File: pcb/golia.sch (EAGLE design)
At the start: 23 parts, among them IC1 xm64a4u, IC2 LM340MP, X2 EXT

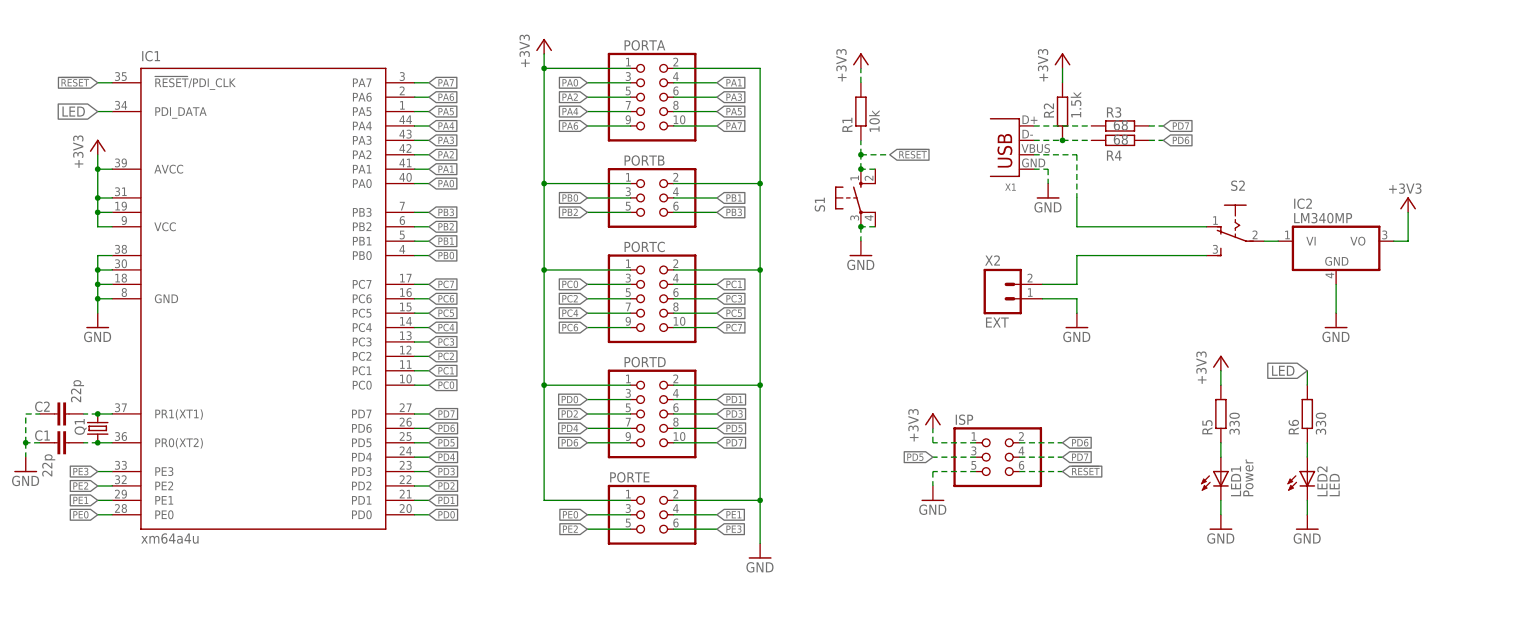
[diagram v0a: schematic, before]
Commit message: Changed component packages
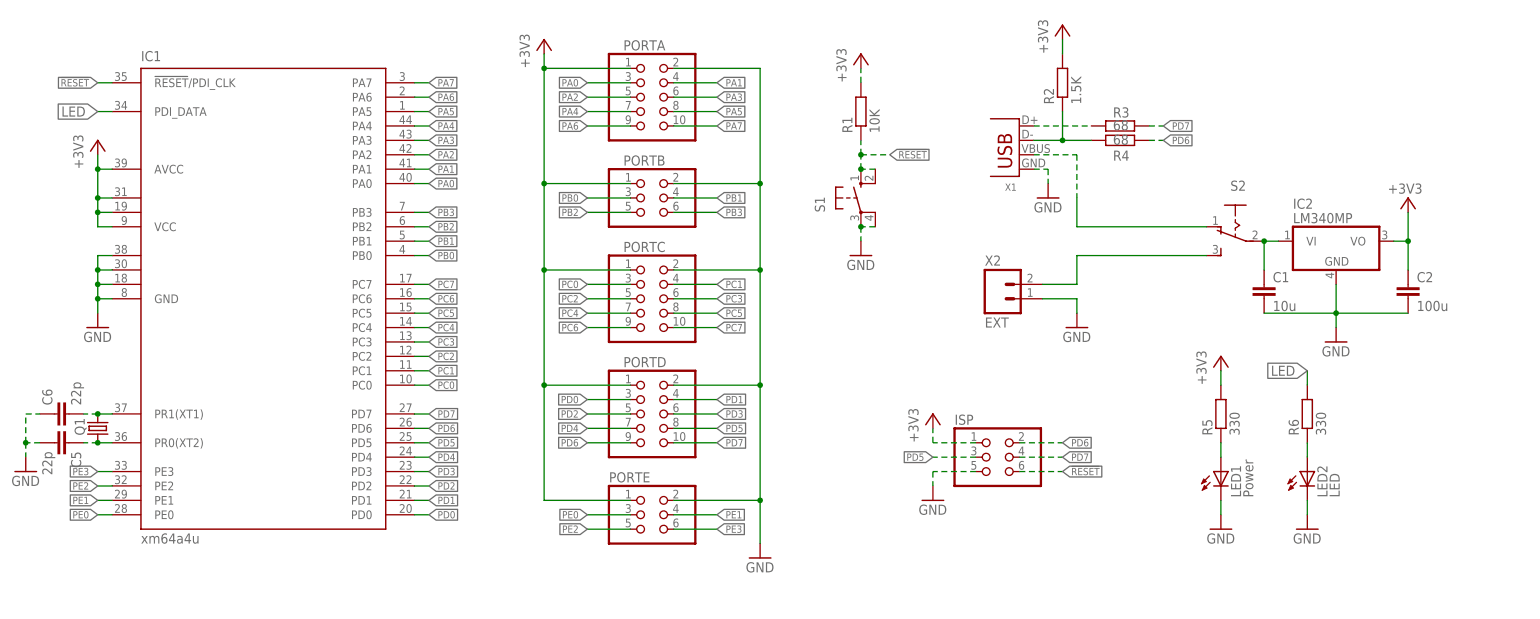
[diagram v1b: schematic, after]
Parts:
- added C5, C6: 22p, Passives:C0603
- C1: value 22p -> 10u; device resistor:C-EU025-024X044 -> Passives:C0603
- C2: value 22p -> 100u; device resistor:C-EU025-024X044 -> rcl:C-EUC1206
- R1: value 10k -> 10K; device resistor:R-EU_M0805 -> rcl:R-EU_R0603
- R2: value 1.5k -> 1.5K; device resistor:R-EU_M0805 -> rcl:R-EU_R0603
- R3, R4: device resistor:R-EU_M0805 -> rcl:R-EU_R0603
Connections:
- net +3V3: now also C2.1
- net GND: now also C1.2, C2.2, C5.2, C6.1; no longer C1.1, C2.1
- net N$23: now also C5.1; no longer C1.2
- net N$24: now also C6.2; no longer C2.2
- net N$5: now also C1.1
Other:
- moved on the sheet: C1, C2, R2

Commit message: Changed layout of board, USB now central
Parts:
- R5, R6: device resistor:R-EU_M0805 -> rcl:R-EU_R0603
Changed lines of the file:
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@@
 <part name="GND1" library="supply1" deviceset="GND" device=""/>
 <part name="GND9" library="supply1" deviceset="GND" device=""/>
-<part name="R5" library="resistor" deviceset="R-EU_" device="M0805" value="330"/>
-<part name="R6" library="resistor" deviceset="R-EU_" device="M0805" value="330"/>
+<part name="R5" library="rcl" deviceset="R-EU_" device="R0603" value="330"/>
+<part name="R6" library="rcl" deviceset="R-EU_" device="R0603" value="330"/>
 <part name="LED1" library="led" deviceset="LED" device="CHIP-LED0805" value="Power"/>
 <part name="LED2" library="led" deviceset="LED" device="CHIP-LED0805" value="LED"/>

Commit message: Added Silkscreen for ports
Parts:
- LED1: value Power -> PWR
- renumbered PORTA to A, PORTB to B, PORTC to C, PORTD to D, PORTE to E

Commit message: * Swapped out the power switch, regulator, and USB connector with those available free from the uni * Fattened up some of the power supply traces.
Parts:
- removed IC2: LM340MP, linear:LM340MP-05
- removed S2: (no value), switch:255SB
- removed X1: (no value), con-usb-3:USB-MB-S
- added S3: SPDTEG-1218, Switches:SPDTEG-1218
- added U$1: USB-MINIB-PTH, Connectors:USB-MINIB-PTH
- added U1: MCP1825S-3302E/DB, mcp1825:MCP1825S-3302E/DB
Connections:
- net +3V3: now also U1.VOUT; no longer IC2.VO
- net GND: now also U$1.GND, U$1.SHD1, U$1.SHD2, U1.GND, U1.GND_TAB; no longer IC2.GND, X1.GND
- net N$1: now also S3.1; no longer S2.S
- net N$2: now also S3.2, U$1.VBUS; no longer S2.O, X1.VBUS
- net N$3: now also U$1.D-; no longer X1.D-
- net N$4: now also U$1.D+; no longer X1.D+
- net N$5: now also S3.C, U1.VIN; no longer IC2.VI, S2.P
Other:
- moved on the sheet: C1, C2, ISP, LED1, LED2, R5, R6

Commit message: Added names to silk screen increased board size to fit port silks
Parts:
- S: value SPDTEG-1218 -> 3
- renumbered S3 to S
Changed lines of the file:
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@@
 <?xml version="1.0" encoding="utf-8"?>
 <!DOCTYPE eagle SYSTEM "eagle.dtd">
-<eagle version="7.7.0">
+<eagle version="8.1.0">
 <drawing>
 <settings>
@@
 <part name="R3" library="rcl" deviceset="R-EU_" device="R0603" value="68"/>
 <part name="R4" library="rcl" deviceset="R-EU_" device="R0603" value="68"/>
-<part name="S3" library="Switches" deviceset="SPDT" device="EG-1218"/>
+<part name="S" library="Switches" deviceset="SPDT" device="EG-1218" value="3"/>
 <part name="U$1" library="Connectors" deviceset="USB-MINI" device="B-PTH"/>
 <part name="GND10" library="supply1" deviceset="GND" device=""/>
@@
 <attribute name="VALUE" x="171.45" y="67.818" size="1.778" layer="96"/>
 </instance>
-<instance part="S3" gate="G$1" x="193.04" y="50.8" rot="R180"/>
+<instance part="S" gate="G$1" x="193.04" y="50.8" rot="R180"/>
 <instance part="U$1" gate="G$1" x="152.4" y="66.04" rot="MR0"/>
 <instance part="GND10" gate="1" x="147.32" y="53.34"/>
@@
 <wire x1="165.1" y1="58.42" x2="165.1" y2="53.34" width="0.1524" layer="91"/>
 <wire x1="165.1" y1="53.34" x2="187.96" y2="53.34" width="0.1524" layer="91"/>
-<pinref part="S3" gate="G$1" pin="2"/>
+<pinref part="S" gate="G$1" pin="2"/>
 <pinref part="U$1" gate="G$1" pin="VBUS"/>
 </segment>
@@
 <pinref part="X2" gate="G$1" pin="2"/>
 <wire x1="159.004" y1="43.18" x2="165.1" y2="43.18" width="0.1524" layer="91"/>
-<pinref part="S3" gate="G$1" pin="1"/>
+<pinref part="S" gate="G$1" pin="1"/>
 </segment>
 </net>
@@
 <wire x1="198.12" y1="40.64" x2="198.12" y2="50.8" width="0.1524" layer="91"/>
 <pinref part="C1" gate="G$1" pin="1"/>
-<pinref part="S3" gate="G$1" pin="C"/>
+<pinref part="S" gate="G$1" pin="C"/>
 <junction x="198.12" y="50.8"/>
 <pinref part="U1" gate="A" pin="VIN"/>

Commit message: Changes to LEDs
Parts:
- removed C5, C6: 22p, Passives:C0603
- removed Q1: (no value), adafruit:CRYSTALCTS406
- added LED3: LED1, led:LEDCHIP-LED0805
- added R7: 330, rcl:R-EU_R0603
- LED2: value LED -> LED2
- renumbered U$1 to USB
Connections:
- removed net LED: IC1.PDI_DATA, R6.2
- removed net N$23: C5.1, IC1.PR0(XT2), Q1.1
- removed net N$24: C6.2, IC1.PR1(XT1), Q1.2
- new net LED1: IC1.PR1(XT1), R6.2
- new net LED2: IC1.PR0(XT2), R7.2
- new net N$10: LED3.A, R7.1
- net GND: now also LED3.C; no longer C5.2, C6.1
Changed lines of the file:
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@@
 <part name="+3V4" library="supply1" deviceset="+3V3" device=""/>
 <part name="GND4" library="supply1" deviceset="GND" device=""/>
-<part name="GND5" library="supply1" deviceset="GND" device=""/>
-<part name="Q1" library="adafruit" deviceset="CRYSTAL" device="CTS406"/>
 <part name="GND6" library="supply1" deviceset="GND" device=""/>
 <part name="+3V5" library="supply1" deviceset="+3V3" device=""/>
@@
 <part name="R6" library="rcl" deviceset="R-EU_" device="R0603" value="330"/>
 <part name="LED1" library="led" deviceset="LED" device="CHIP-LED0805" value="PWR"/>
-<part name="LED2" library="led" deviceset="LED" device="CHIP-LED0805" value="LED"/>
-<part name="C5" library="Passives" deviceset="C" device="0603" value="22p"/>
-<part name="C6" library="Passives" deviceset="C" device="0603" value="22p"/>
+<part name="LED2" library="led" deviceset="LED" device="CHIP-LED0805" value="LED2"/>
 <part name="C1" library="Passives" deviceset="C" device="0603" value="10u"/>
 <part name="C2" library="rcl" deviceset="C-EU" device="C1206" value="100u"/>
@@
 <part name="R4" library="rcl" deviceset="R-EU_" device="R0603" value="68"/>
 <part name="S" library="Switches" deviceset="SPDT" device="EG-1218" value="3"/>
-<part name="U$1" library="Connectors" deviceset="USB-MINI" device="B-PTH"/>
+<part name="USB" library="Connectors" deviceset="USB-MINI" device="B-PTH"/>
 <part name="GND10" library="supply1" deviceset="GND" device=""/>
 <part name="GND11" library="supply1" deviceset="GND" device=""/>
 <part name="U1" library="mcp1825" deviceset="MCP1825S-3302E/DB" device=""/>
+<part name="R7" library="rcl" deviceset="R-EU_" device="R0603" value="330"/>
+<part name="LED3" library="led" deviceset="LED" device="CHIP-LED0805" value="LED1"/>
+<part name="GND5" library="supply1" deviceset="GND" device=""/>
 </parts>
 <sheets>
@@
 <instance part="+3V4" gate="G$1" x="139.7" y="10.16"/>
 <instance part="GND4" gate="1" x="139.7" y="-5.08"/>
-<instance part="GND5" gate="1" x="-20.32" y="10.16"/>
-<instance part="Q1" gate="G$1" x="-7.62" y="17.78" smashed="yes" rot="R90">
-<attribute name="NAME" x="-9.906" y="16.51" size="1.778" layer="95" rot="R90"/>
-<attribute name="VALUE" x="-5.08" y="20.32" size="1.778" layer="96" rot="R90"/>
-</instance>
 <instance part="GND6" gate="1" x="160.02" y="58.42"/>
 <instance part="+3V5" gate="G$1" x="162.56" y="88.9"/>
@@
 <instance part="LED1" gate="G$1" x="190.5" y="0"/>
 <instance part="LED2" gate="G$1" x="205.74" y="0"/>
-<instance part="C5" gate="G$1" x="-12.7" y="15.24" rot="R270"/>
-<instance part="C6" gate="G$1" x="-15.24" y="20.32" rot="R90"/>
 <instance part="C1" gate="G$1" x="198.12" y="38.1"/>
 <instance part="C2" gate="G$1" x="236.22" y="38.1"/>
@@
 </instance>
 <instance part="S" gate="G$1" x="193.04" y="50.8" rot="R180"/>
-<instance part="U$1" gate="G$1" x="152.4" y="66.04" rot="MR0"/>
+<instance part="USB" gate="G$1" x="152.4" y="66.04" smashed="yes" rot="MR0">
+<attribute name="NAME" x="144.78" y="73.66" size="1.778" layer="95" rot="MR0"/>
+</instance>
 <instance part="GND10" gate="1" x="147.32" y="53.34"/>
 <instance part="GND11" gate="1" x="152.4" y="76.2"/>
 <instance part="U1" gate="A" x="220.98" y="53.34"/>
+<instance part="R7" gate="G$1" x="220.98" y="10.16" rot="R90"/>
+<instance part="LED3" gate="G$1" x="220.98" y="0"/>
+<instance part="GND5" gate="1" x="220.98" y="-10.16"/>
 </instances>
 <busses>
@@
 </segment>
 <segment>
-<wire x1="-17.78" y1="15.24" x2="-20.32" y2="15.24" width="0.1524" layer="91" style="longdash"/>
-<wire x1="-20.32" y1="15.24" x2="-20.32" y2="20.32" width="0.1524" layer="91" style="longdash"/>
-<wire x1="-20.32" y1="20.32" x2="-17.78" y2="20.32" width="0.1524" layer="91" style="longdash"/>
-<wire x1="-20.32" y1="15.24" x2="-20.32" y2="12.7" width="0.1524" layer="91" style="longdash"/>
-<junction x="-20.32" y="15.24"/>
-<pinref part="GND5" gate="1" pin="GND"/>
-<pinref part="C6" gate="G$1" pin="1"/>
-<pinref part="C5" gate="G$1" pin="2"/>
-</segment>
-<segment>
 <wire x1="157.48" y1="63.5" x2="160.02" y2="63.5" width="0.1524" layer="91" style="longdash"/>
 <wire x1="160.02" y1="63.5" x2="160.02" y2="60.96" width="0.1524" layer="91" style="longdash"/>
 <pinref part="GND6" gate="1" pin="GND"/>
-<pinref part="U$1" gate="G$1" pin="GND"/>
+<pinref part="USB" gate="G$1" pin="GND"/>
 </segment>
 <segment>
@@
 <pinref part="GND11" gate="1" pin="GND"/>
 <wire x1="152.4" y1="81.28" x2="152.4" y2="78.74" width="0.1524" layer="91"/>
-<pinref part="U$1" gate="G$1" pin="SHD1"/>
-</segment>
-<segment>
-<pinref part="U$1" gate="G$1" pin="SHD2"/>
+<pinref part="USB" gate="G$1" pin="SHD1"/>
+</segment>
+<segment>
+<pinref part="USB" gate="G$1" pin="SHD2"/>
 <pinref part="GND10" gate="1" pin="GND"/>
 <wire x1="147.32" y1="57.15" x2="147.32" y2="55.88" width="0.1524" layer="91"/>
+</segment>
+<segment>
+<pinref part="GND5" gate="1" pin="GND"/>
+<pinref part="LED3" gate="G$1" pin="C"/>
+<wire x1="220.98" y1="-7.62" x2="220.98" y2="-5.08" width="0.1524" layer="91"/>
 </segment>
 </net>
@@
 <wire x1="101.6" y1="2.54" x2="93.98" y2="2.54" width="0.1524" layer="91"/>
 <label x="101.6" y="2.54" size="1.27" layer="95" xref="yes"/>
-</segment>
-</net>
-<net name="N$23" class="0">
-<segment>
-<pinref part="IC1" gate="G$1" pin="PR0(XT2)"/>
-<wire x1="-5.08" y1="15.24" x2="-7.62" y2="15.24" width="0.1524" layer="91"/>
-<wire x1="-7.62" y1="15.24" x2="-10.16" y2="15.24" width="0.1524" layer="91" style="longdash"/>
-<pinref part="Q1" gate="G$1" pin="1"/>
-<junction x="-7.62" y="15.24"/>
-<pinref part="C5" gate="G$1" pin="1"/>
-</segment>
-</net>
-<net name="N$24" class="0">
-<segment>
-<pinref part="IC1" gate="G$1" pin="PR1(XT1)"/>
-<wire x1="-5.08" y1="20.32" x2="-7.62" y2="20.32" width="0.1524" layer="91"/>
-<wire x1="-7.62" y1="20.32" x2="-10.16" y2="20.32" width="0.1524" layer="91" style="longdash"/>
-<pinref part="Q1" gate="G$1" pin="2"/>
-<junction x="-7.62" y="20.32"/>
-<pinref part="C6" gate="G$1" pin="2"/>
 </segment>
 </net>
@@
 <wire x1="165.1" y1="53.34" x2="187.96" y2="53.34" width="0.1524" layer="91"/>
 <pinref part="S" gate="G$1" pin="2"/>
-<pinref part="U$1" gate="G$1" pin="VBUS"/>
+<pinref part="USB" gate="G$1" pin="VBUS"/>
 </segment>
 </net>
@@
 <wire x1="157.48" y1="71.12" x2="167.64" y2="71.12" width="0.1524" layer="91" style="longdash"/>
 <pinref part="R3" gate="G$1" pin="1"/>
-<pinref part="U$1" gate="G$1" pin="D+"/>
+<pinref part="USB" gate="G$1" pin="D+"/>
 </segment>
 </net>
@@
 </segment>
 </net>
-<net name="LED" class="0">
-<segment>
-<pinref part="IC1" gate="G$1" pin="PDI_DATA"/>
-<wire x1="-5.08" y1="73.66" x2="-7.62" y2="73.66" width="0.1524" layer="91"/>
-<label x="-7.62" y="73.66" size="1.778" layer="95" rot="MR0" xref="yes"/>
-</segment>
-<segment>
-<pinref part="R6" gate="G$1" pin="2"/>
-<wire x1="205.74" y1="15.24" x2="205.74" y2="17.78" width="0.1524" layer="91"/>
-<label x="205.74" y="17.78" size="1.778" layer="95" rot="R180" xref="yes"/>
-</segment>
-</net>
 <net name="N$3" class="0">
 <segment>
@@
 <pinref part="R2" gate="G$1" pin="1"/>
 <pinref part="R4" gate="G$1" pin="1"/>
-<pinref part="U$1" gate="G$1" pin="D-"/>
-</segment>
-</net>
+<pinref part="USB" gate="G$1" pin="D-"/>
+</segment>
+</net>
+<net name="LED1" class="0">
+<segment>
+<pinref part="IC1" gate="G$1" pin="PR1(XT1)"/>
+<wire x1="-5.08" y1="20.32" x2="-7.62" y2="20.32" width="0.1524" layer="91"/>
+<label x="-7.62" y="20.32" size="1.778" layer="95" rot="R180" xref="yes"/>
+</segment>
+<segment>
+<pinref part="R6" gate="G$1" pin="2"/>
+<wire x1="205.74" y1="15.24" x2="205.74" y2="17.78" width="0.1524" layer="91"/>
+<label x="205.74" y="17.78" size="1.778" layer="95" rot="R180" xref="yes"/>
+<wire x1="205.74" y1="15.24" x2="205.74" y2="17.78" width="0.1524" layer="91"/>
+</segment>
+</net>
+<net name="LED2" class="0">
+<segment>
+<pinref part="IC1" gate="G$1" pin="PR0(XT2)"/>
+<wire x1="-5.08" y1="15.24" x2="-7.62" y2="15.24" width="0.1524" layer="91"/>
+<label x="-7.62" y="15.24" size="1.778" layer="95" rot="R180" xref="yes"/>
+</segment>
+<segment>
+<pinref part="R7" gate="G$1" pin="2"/>
+<wire x1="220.98" y1="15.24" x2="220.98" y2="17.78" width="0.1524" layer="91"/>
+<label x="220.98" y="17.78" size="1.778" layer="95" rot="R180" xref="yes"/>
+</segment>
+</net>
+<net name="N$10" class="0">
+<segment>
+<pinref part="R7" gate="G$1" pin="1"/>
+<pinref part="LED3" gate="G$1" pin="A"/>
+<wire x1="220.98" y1="5.08" x2="220.98" y2="2.54" width="0.1524" layer="91"/>
+</segment>
+</net>

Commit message: Reduced width and removed !RST pullup
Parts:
- removed R1: 10K, rcl:R-EU_R0603
- S3: value 3 -> S3
- renumbered S to S3
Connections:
- net !RESET: no longer R1.1
- net +3V3: no longer R1.2
- net LED1: now also IC1.PR0(XT2), R7.2; no longer IC1.PR1(XT1), R6.2
- net LED2: now also IC1.PR1(XT1), R6.2; no longer IC1.PR0(XT2), R7.2
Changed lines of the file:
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@@
 <part name="A" library="pinhead" deviceset="PINHD-2X5" device=""/>
 <part name="S1" library="switch-omron" deviceset="10-XX" device=""/>
-<part name="+3V3" library="supply1" deviceset="+3V3" device=""/>
 <part name="GND3" library="supply1" deviceset="GND" device=""/>
 <part name="ISP" library="pinhead" deviceset="PINHD-2X3" device=""/>
@@
 <part name="C1" library="Passives" deviceset="C" device="0603" value="10u"/>
 <part name="C2" library="rcl" deviceset="C-EU" device="C1206" value="100u"/>
-<part name="R1" library="rcl" deviceset="R-EU_" device="R0603" value="10K"/>
 <part name="R2" library="rcl" deviceset="R-EU_" device="R0603" value="1.5K"/>
 <part name="R3" library="rcl" deviceset="R-EU_" device="R0603" value="68"/>
 <part name="R4" library="rcl" deviceset="R-EU_" device="R0603" value="68"/>
-<part name="S" library="Switches" deviceset="SPDT" device="EG-1218" value="3"/>
+<part name="S3" library="Switches" deviceset="SPDT" device="EG-1218" value="S3"/>
 <part name="USB" library="Connectors" deviceset="USB-MINI" device="B-PTH"/>
 <part name="GND10" library="supply1" deviceset="GND" device=""/>
@@
 </instance>
 <instance part="E" gate="A" x="88.9" y="2.54" smashed="yes">
-<attribute name="NAME" x="82.55" y="8.255" size="1.778" layer="95"/>
+<attribute name="NAME" x="85.09" y="8.255" size="1.778" layer="95"/>
 <attribute name="VALUE" x="82.55" y="-5.08" size="1.778" layer="96"/>
 </instance>
@@
 </instance>
 <instance part="S1" gate="1" x="127" y="58.42"/>
-<instance part="+3V3" gate="G$1" x="127" y="83.82"/>
 <instance part="GND3" gate="1" x="127" y="48.26"/>
 <instance part="ISP" gate="A" x="149.86" y="2.54"/>
@@
 <instance part="C1" gate="G$1" x="198.12" y="38.1"/>
 <instance part="C2" gate="G$1" x="236.22" y="38.1"/>
-<instance part="R1" gate="G$1" x="127" y="73.66" rot="R90"/>
 <instance part="R2" gate="G$1" x="162.56" y="78.74" rot="R90"/>
 <instance part="R3" gate="G$1" x="172.72" y="71.12" smashed="yes">
@@
 <attribute name="VALUE" x="171.45" y="67.818" size="1.778" layer="96"/>
 </instance>
-<instance part="S" gate="G$1" x="193.04" y="50.8" rot="R180"/>
+<instance part="S3" gate="G$1" x="193.04" y="50.8" rot="R180"/>
 <instance part="USB" gate="G$1" x="152.4" y="66.04" smashed="yes" rot="MR0">
 <attribute name="NAME" x="144.78" y="73.66" size="1.778" layer="95" rot="MR0"/>
@@
 </segment>
 <segment>
-<wire x1="127" y1="78.74" x2="127" y2="81.28" width="0.1524" layer="91" style="longdash"/>
-<pinref part="+3V3" gate="G$1" pin="+3V3"/>
-<pinref part="R1" gate="G$1" pin="2"/>
-</segment>
-<segment>
 <pinref part="ISP" gate="A" pin="1"/>
 <wire x1="147.32" y1="5.08" x2="139.7" y2="5.08" width="0.1524" layer="91" style="longdash"/>
@@
 <wire x1="129.54" y1="63.5" x2="127" y2="63.5" width="0.1524" layer="91" style="longdash"/>
 <junction x="127" y="63.5"/>
-<wire x1="127" y1="63.5" x2="127" y2="66.04" width="0.1524" layer="91" style="longdash"/>
-<wire x1="127" y1="66.04" x2="127" y2="68.58" width="0.1524" layer="91" style="longdash"/>
-<wire x1="127" y1="66.04" x2="132.08" y2="66.04" width="0.1524" layer="91" style="longdash"/>
-<junction x="127" y="66.04"/>
-<label x="132.08" y="66.04" size="1.27" layer="95" xref="yes"/>
-<pinref part="R1" gate="G$1" pin="1"/>
+<wire x1="127" y1="63.5" x2="127" y2="71.12" width="0.1524" layer="91" style="longdash"/>
+<label x="127" y="71.12" size="1.27" layer="95" rot="R180" xref="yes"/>
 </segment>
 </net>
@@
 <wire x1="165.1" y1="58.42" x2="165.1" y2="53.34" width="0.1524" layer="91"/>
 <wire x1="165.1" y1="53.34" x2="187.96" y2="53.34" width="0.1524" layer="91"/>
-<pinref part="S" gate="G$1" pin="2"/>
+<pinref part="S3" gate="G$1" pin="2"/>
 <pinref part="USB" gate="G$1" pin="VBUS"/>
 </segment>
@@
 <pinref part="X2" gate="G$1" pin="2"/>
 <wire x1="159.004" y1="43.18" x2="165.1" y2="43.18" width="0.1524" layer="91"/>
-<pinref part="S" gate="G$1" pin="1"/>
+<pinref part="S3" gate="G$1" pin="1"/>
 </segment>
 </net>
@@
 <wire x1="198.12" y1="40.64" x2="198.12" y2="50.8" width="0.1524" layer="91"/>
 <pinref part="C1" gate="G$1" pin="1"/>
-<pinref part="S" gate="G$1" pin="C"/>
+<pinref part="S3" gate="G$1" pin="C"/>
 <junction x="198.12" y="50.8"/>
 <pinref part="U1" gate="A" pin="VIN"/>
@@
 </segment>
 </net>
-<net name="LED1" class="0">
+<net name="LED2" class="0">
 <segment>
 <pinref part="IC1" gate="G$1" pin="PR1(XT1)"/>
@@
 <segment>
 <pinref part="R6" gate="G$1" pin="2"/>
-<wire x1="205.74" y1="15.24" x2="205.74" y2="17.78" width="0.1524" layer="91"/>
 <label x="205.74" y="17.78" size="1.778" layer="95" rot="R180" xref="yes"/>
 <wire x1="205.74" y1="15.24" x2="205.74" y2="17.78" width="0.1524" layer="91"/>
 </segment>
 </net>
-<net name="LED2" class="0">
+<net name="LED1" class="0">
 <segment>
 <pinref part="IC1" gate="G$1" pin="PR0(XT2)"/>
